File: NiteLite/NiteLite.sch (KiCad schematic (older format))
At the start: 13 parts, among them J1 USB_B_Micro, J2 USB_A, U1 7555, U2 TLV1117-33, X1 Badgelife_sao_connector_v169b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

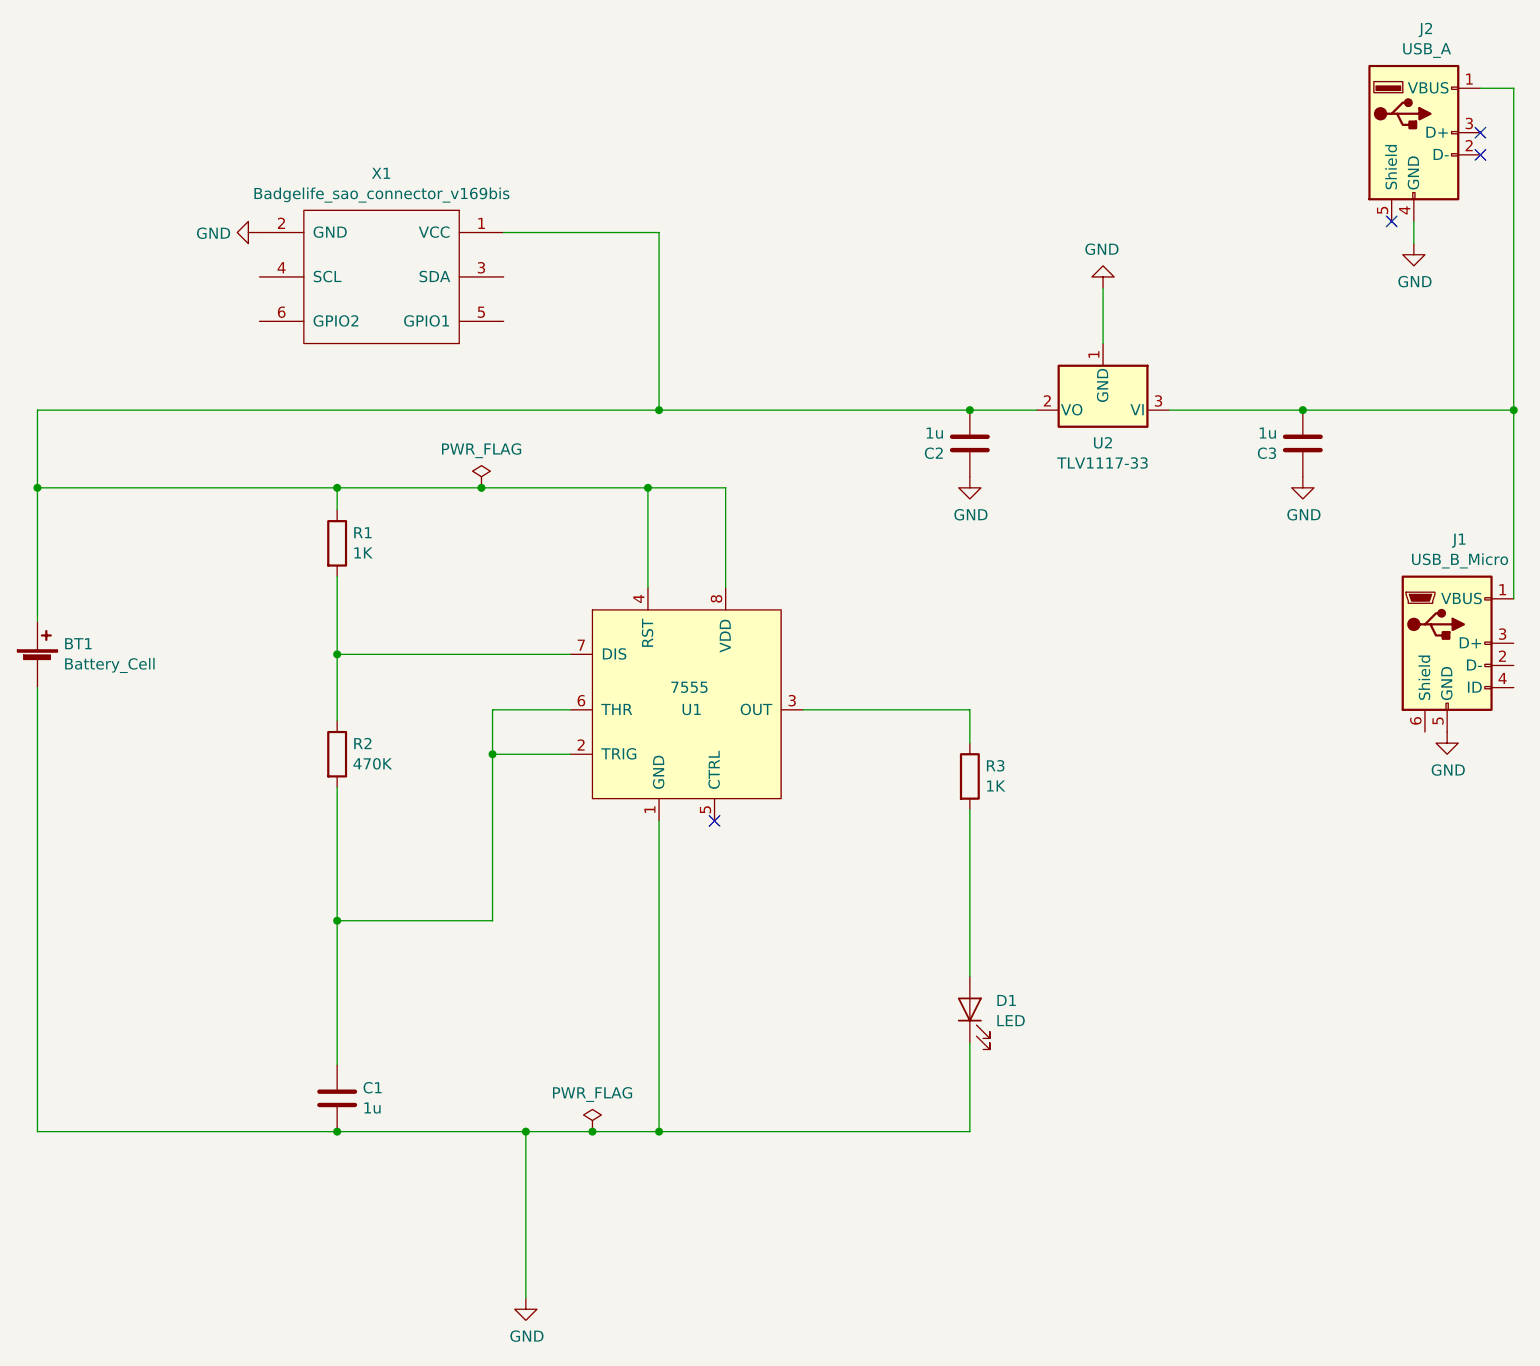
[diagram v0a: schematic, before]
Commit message: updates to artwork and sch
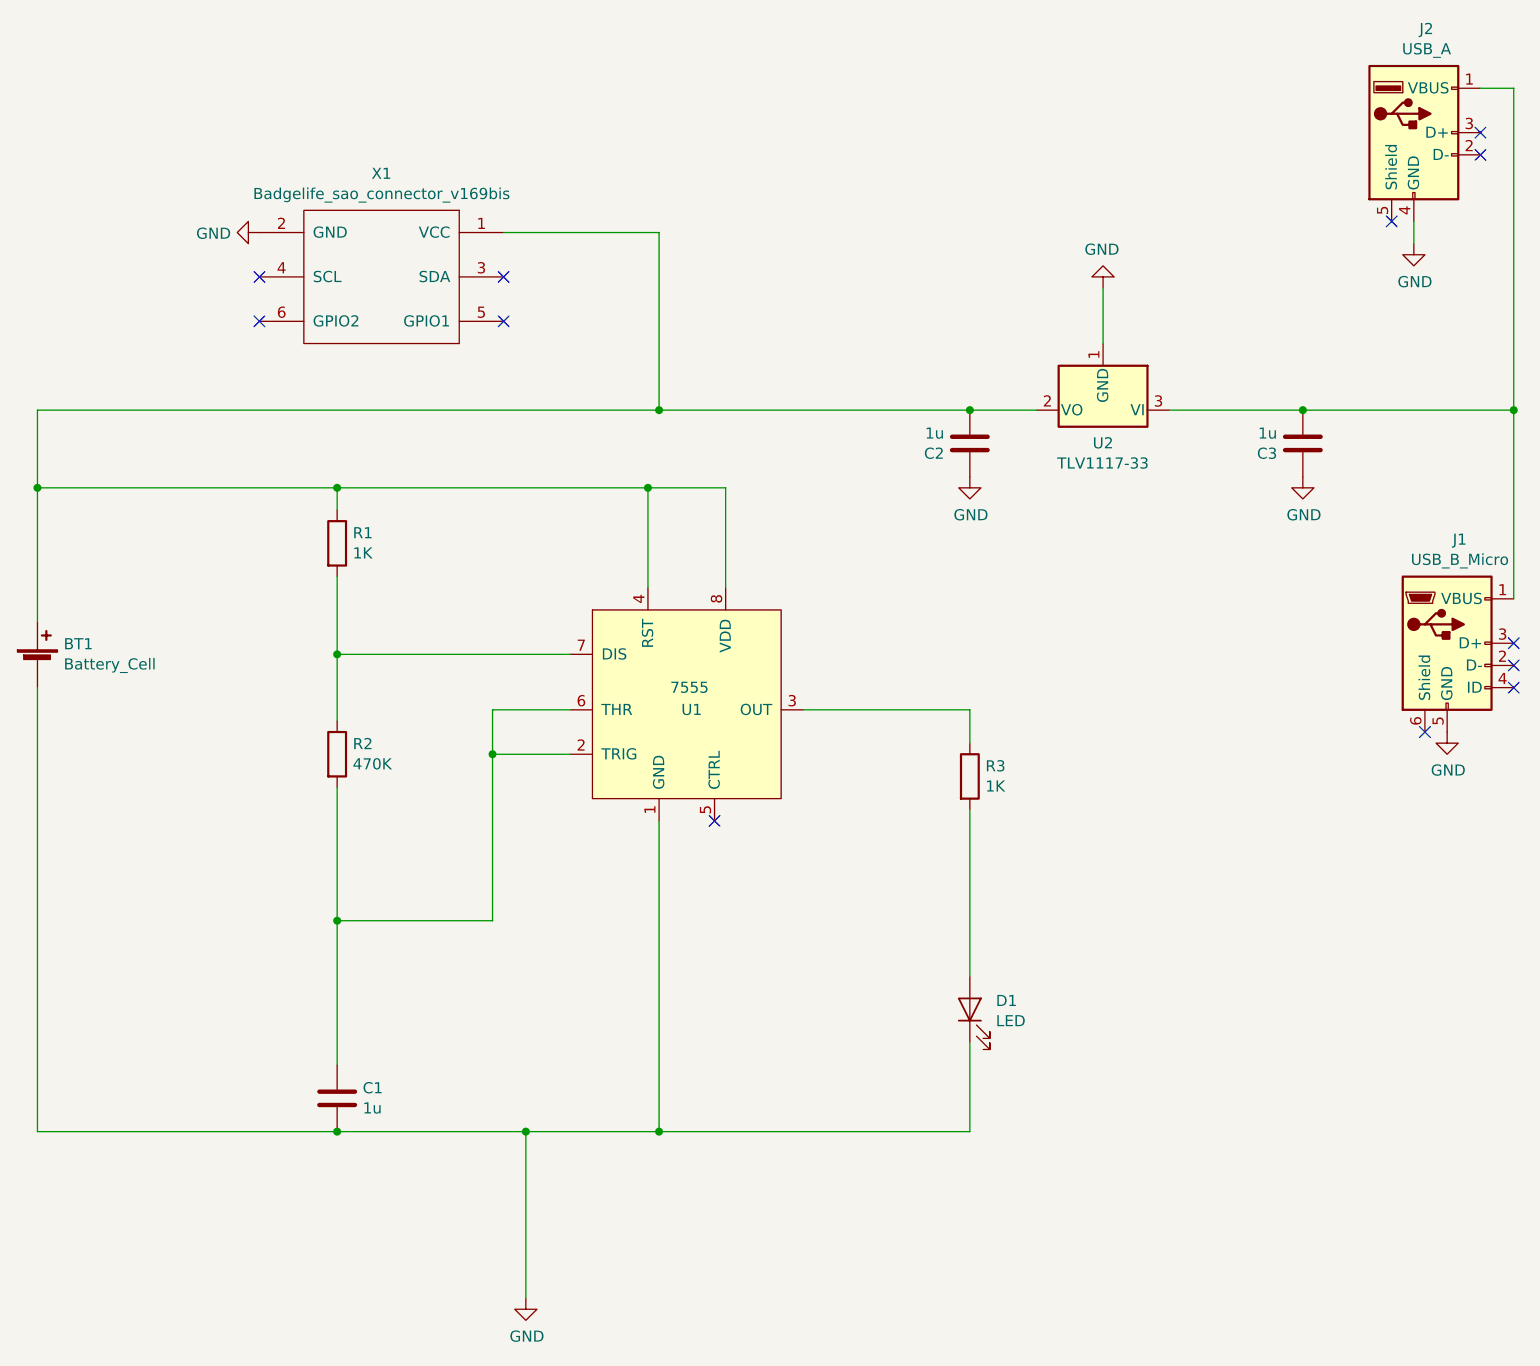
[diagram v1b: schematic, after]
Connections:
- no-connect marks 4 -> 12
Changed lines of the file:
@@
 Connection ~ 4350 2600
-Wire Wire Line
-	4350 2600 5000 2600
 Wire Wire Line
 	4350 3950 4350 4550
@@
 	7200 3750 7200 3600
 Connection ~ 5200 5500
-Wire Wire Line
-	5200 5500 5500 5500
 Wire Wire Line
 	7200 4800 7200 4050
@@
 	1    0    0    -1
 $EndComp
-$Comp
-L power:PWR_FLAG #FLG0101
-U 1 1 5DC91944
-P 5000 2600
-F 0 "#FLG0101" H 5000 2675 50  0001 C CNN
-F 1 "PWR_FLAG" H 5000 2773 50  0000 C CNN
-F 2 "" H 5000 2600 50  0001 C CNN
-F 3 "~" H 5000 2600 50  0001 C CNN
-	1    5000 2600
-	1    0    0    -1
-$EndComp
-Connection ~ 5000 2600
-Wire Wire Line
-	5000 2600 5750 2600
-$Comp
-L power:PWR_FLAG #FLG0102
-U 1 1 5DC92165
-P 5500 5500
-F 0 "#FLG0102" H 5500 5575 50  0001 C CNN
-F 1 "PWR_FLAG" H 5500 5673 50  0000 C CNN
-F 2 "" H 5500 5500 50  0001 C CNN
-F 3 "~" H 5500 5500 50  0001 C CNN
-	1    5500 5500
-	1    0    0    -1
-$EndComp
-Connection ~ 5500 5500
-Wire Wire Line
-	5500 5500 5800 5500
 Connection ~ 4350 5500
 Wire Wire Line
@@
 	1    0    0    -1
 $EndComp
+NoConn ~ 5100 1650
+NoConn ~ 5100 1850
+NoConn ~ 4000 1850
+NoConn ~ 4000 1650
+NoConn ~ 9650 3300
+NoConn ~ 9650 3400
+NoConn ~ 9650 3500
+NoConn ~ 9250 3700
+Wire Wire Line
+	5200 5500 5800 5500
+Wire Wire Line
+	4350 2600 5750 2600
 $EndSCHEMATC
